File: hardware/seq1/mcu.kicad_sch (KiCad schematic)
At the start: 11 parts, among them SW10 SW_Push, SW11 SW_Push, SW9 PEC12R-3220F-S0024, U5 128x64 0.96" OLED I2C

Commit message: schematic and layout for v1 board
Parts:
- added C17: 1u, Capacitor_THT:C_Disc_D5.0mm_W2.5mm_P5.00mm, symbol Device:C
- added J6: Conn_02x06_Odd_Even, Connector_PinHeader_2.54mm:PinHeader_2x06_P2.54mm_Vertical, symbol Connector_Generic:Conn_02x06_Odd_Even
- added R19, R20: 4.7k, Resistor_THT:R_Axial_DIN0207_L6.3mm_D2.5mm_P10.16mm_Horizontal, symbol Device:R_US
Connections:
- net +3V3: now also R1.1, R2.1, C17.1, J6.1 (Pin_1), J6.2 (Pin_2), R19.1, R20.1; no longer R3.1, R4.1
- net +3V3_A: now also J6.3 (Pin_3)
- net +5V: now also J6.5 (Pin_5)
- net GATE: now also U1.14 (D2/PA14); no longer U1.30 (D13/PA17)
- net GND: now also SW9.S2, C17.2, J6.6 (Pin_6); no longer SW9.S1
- net MUX_ADDR0: now also U1.20 (D0/A6/PA11); no longer U1.29 (D12/PA19)
- net MUX_ADDR1: now also U1.21 (D1/A7/PA10); no longer U1.28 (D11/PA16)
- net MUX_ADDR2: now also U1.25 (D7/PA21); no longer U1.27 (D10/PA18)
- net N_MODE: now also SW10.2, U1.12 (D29/MOSI/PB10); no longer SW11.2, U1.14 (D2/PA14)
- net N_RUN: now also SW11.2; no longer SW10.2
- net ROT_SW: now also SW9.S1, U1.29 (D12/PA19); no longer SW9.S2, U1.10 (D19/A5/PB02)
- net RSWA: now also R3.1, U1.28 (D11/PA16); no longer R1.1, U1.11 (D30/SCK/PB11)
- net RSWB: now also R4.1, U1.27 (D10/PA18); no longer R2.1, U1.12 (D29/MOSI/PB10)
- net MCU_RST: now reaches U1.1 (RST)
- net MCU_RST: now also J6.4 (Pin_4)
- net D3_A9: now reaches U1.18 (D3/A9/PA09)
- net D3_A9: now also J6.12 (Pin_12)
- net D4_A8: now reaches U1.19 (D4/A8/PA08)
- net D4_A8: now also J6.10 (Pin_10)
- net at U1.22 (D26/SDA/PA22), U5.4 (SDA): now also R19.2
- net at U1.23 (D27/SCL/PA23), U5.3 (SCL): now also R20.2
- net D15_A1: now reaches U1.6 (D15/A1/PB08)
- net D15_A1: now also J6.7 (Pin_7)
- net D16_A2: now reaches U1.7 (D16/A2/PB09)
- net D16_A2: now also J6.9 (Pin_9)
- net D17_A3: now reaches U1.8 (D17/A3/PA04)
- net D17_A3: now also J6.11 (Pin_11)
- net at C1.1, R4.2, SW9.A: now also R2.2; no longer R1.2
- net at C2.1, R3.2, SW9.B: now also R1.2; no longer R2.2
- new net D13: J6.8 (Pin_8), U1.30 (D13/PA17)
- new net SYNC_IN: U1.10 (D19/A5/PB02)
- new net SYNC_OUT: U1.11 (D30/SCK/PB11)
- no-connect marks 0 -> 4
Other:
- moved on the sheet: U5

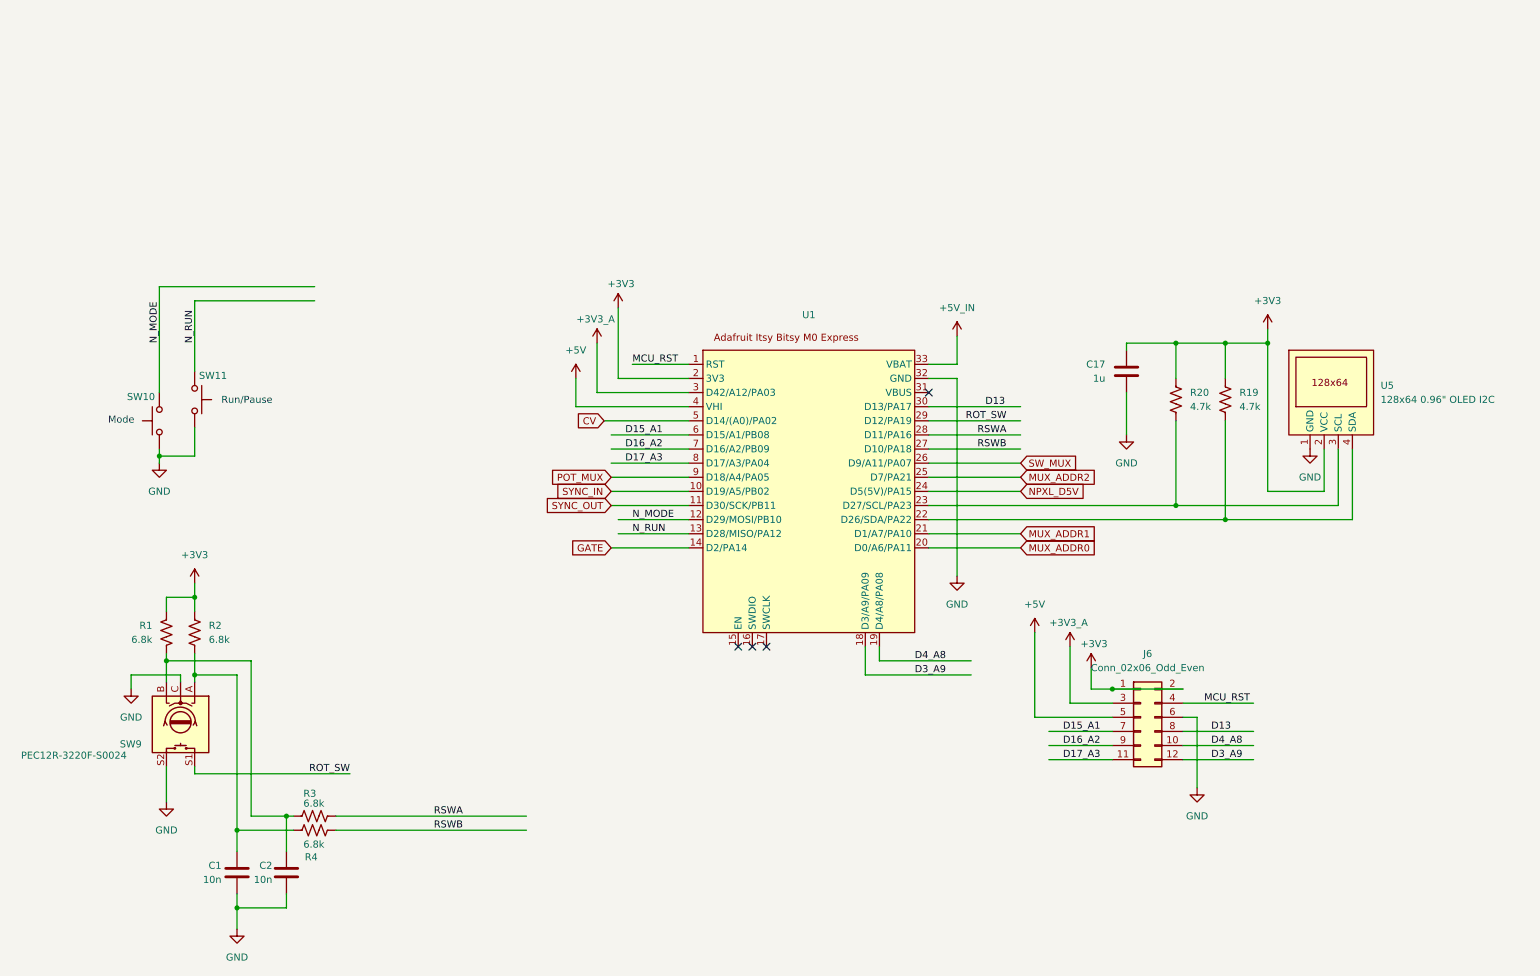
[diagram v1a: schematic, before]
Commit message: Adding support for the Itsy Bitsy M4 (SAMD51) architecture. Removed _util code and refactored to use the SAMD Utilities Library (SAMD_Utils.h). Compiles for QT Py M0, Itsy Bitsy M0 and M4
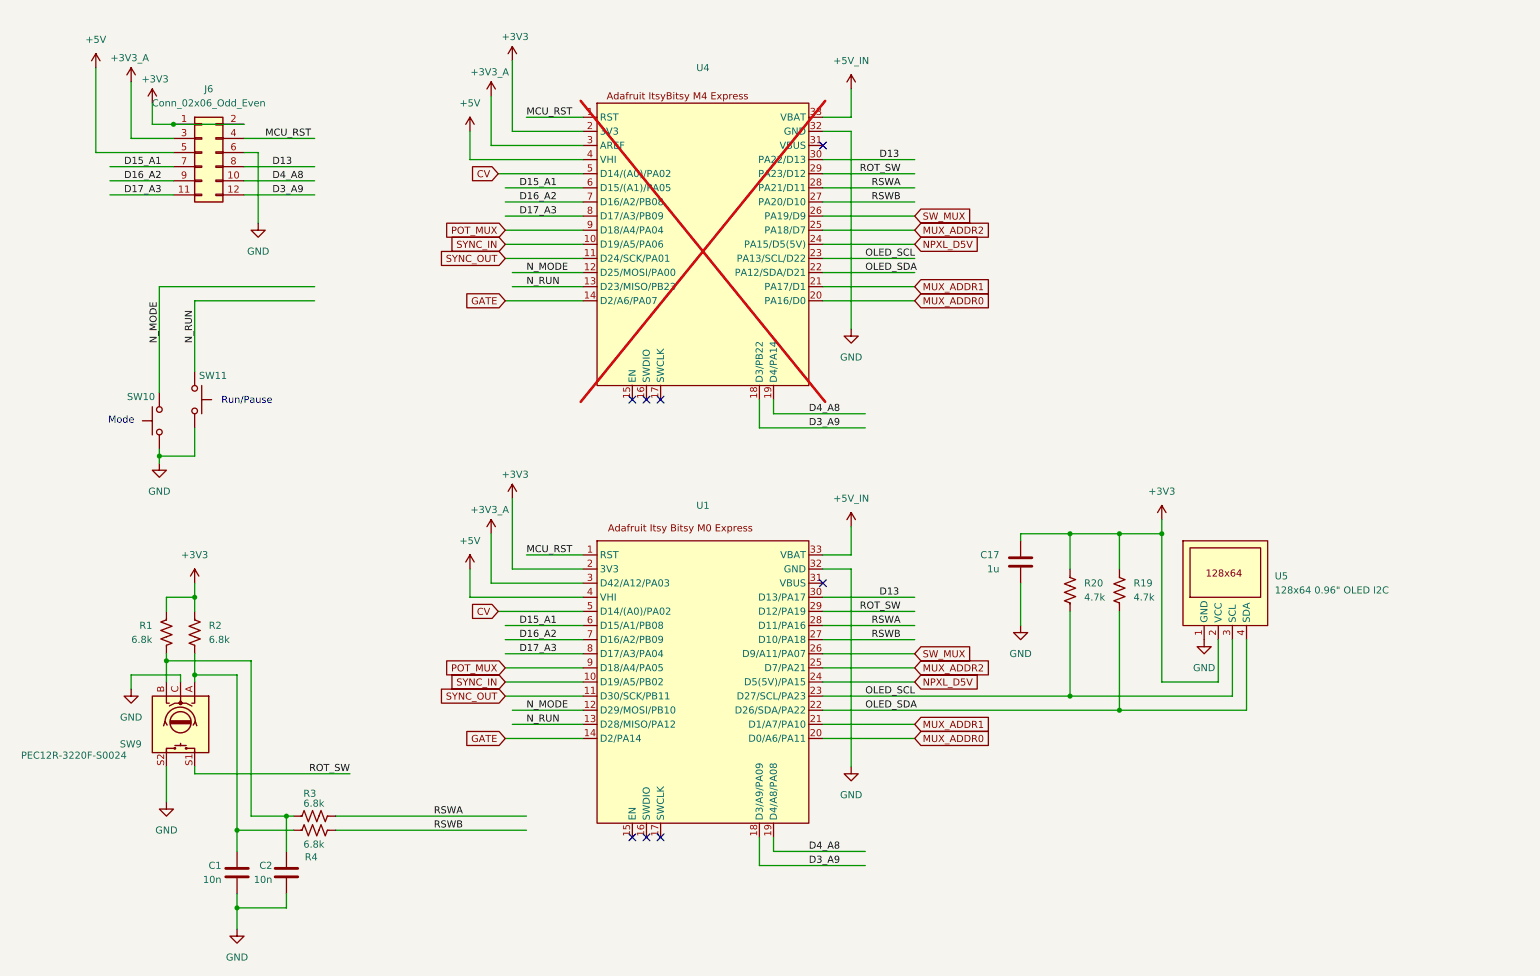
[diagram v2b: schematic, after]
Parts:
- added U4: ~, symbol MCU_Module_Custom:Adafruit_ItsyBitsy_M4_Express
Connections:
- net +3V3: now also U4.2 (3V3)
- net +3V3_A: now also U4.3 (AREF)
- net +5V: now also U4.4 (VHI)
- net +5V_IN: now also U4.33 (VBAT)
- net CV: now also U4.5 (D14/(A0)/PA02)
- net D13: now also U4.30 (PA22/D13)
- net D15_A1: now also U4.6 (D15/(A1)/PA05)
- net D16_A2: now also U4.7 (D16/A2/PB08)
- net D17_A3: now also U4.8 (D17/A3/PB09)
- net D3_A9: now also U4.18 (D3/PB22)
- net D4_A8: now also U4.19 (D4/PA14)
- net GATE: now also U4.14 (D2/A6/PA07)
- net GND: now also U4.32 (GND)
- net MCU_RST: now also U4.1 (RST)
- net MUX_ADDR0: now also U4.20 (PA16/D0)
- net MUX_ADDR1: now also U4.21 (PA17/D1)
- net MUX_ADDR2: now also U4.25 (PA18/D7)
- net NPXL_D5V: now also U4.24 (PA15/D5(5V))
- net N_MODE: now also U4.12 (D25/MOSI/PA00)
- net N_RUN: now also U4.13 (D23/MISO/PB23)
- net POT_MUX: now also U4.9 (D18/A4/PA04)
- net ROT_SW: now also U4.29 (PA23/D12)
- net RSWA: now also U4.28 (PA21/D11)
- net RSWB: now also U4.27 (PA20/D10)
- net SW_MUX: now also U4.26 (PA19/D9)
- net SYNC_IN: now also U4.10 (D19/A5/PA06)
- net SYNC_OUT: now also U4.11 (D24/SCK/PA01)
- net OLED_SDA: now reaches R19.2, U1.22 (D26/SDA/PA22), U5.4 (SDA)
- net OLED_SDA: now also U4.22 (PA12/SDA/D21)
- net OLED_SCL: now reaches R20.2, U1.23 (D27/SCL/PA23), U5.3 (SCL)
- net OLED_SCL: now also U4.23 (PA13/SCL/D22)
- no-connect marks 4 -> 8
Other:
- moved on the sheet: C17, J6, R19, R20, U1, U5

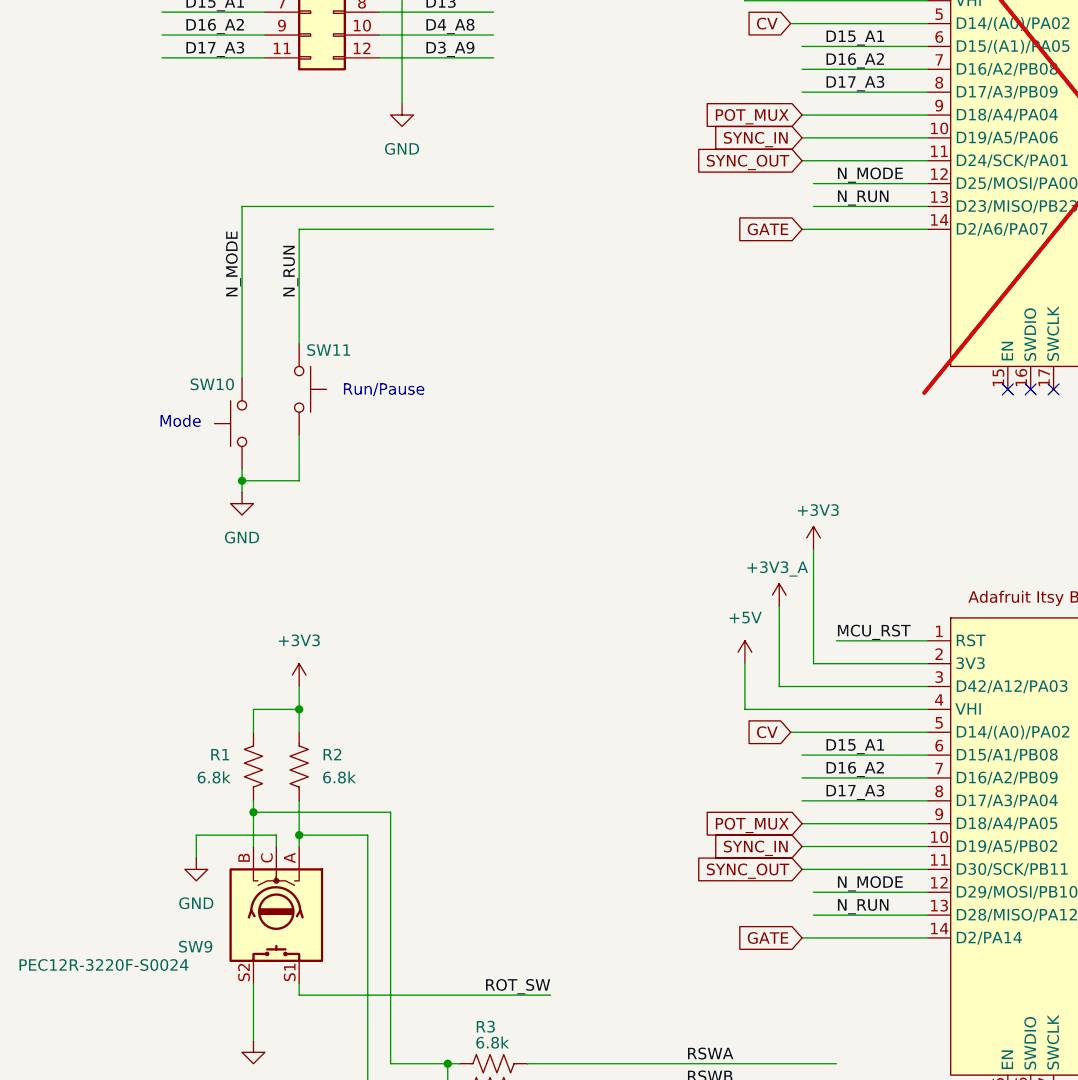
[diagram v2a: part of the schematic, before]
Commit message: bug in layout: order of pots reversed. Fixes for slide algo in controller, pin definitions and other fixes found in testing
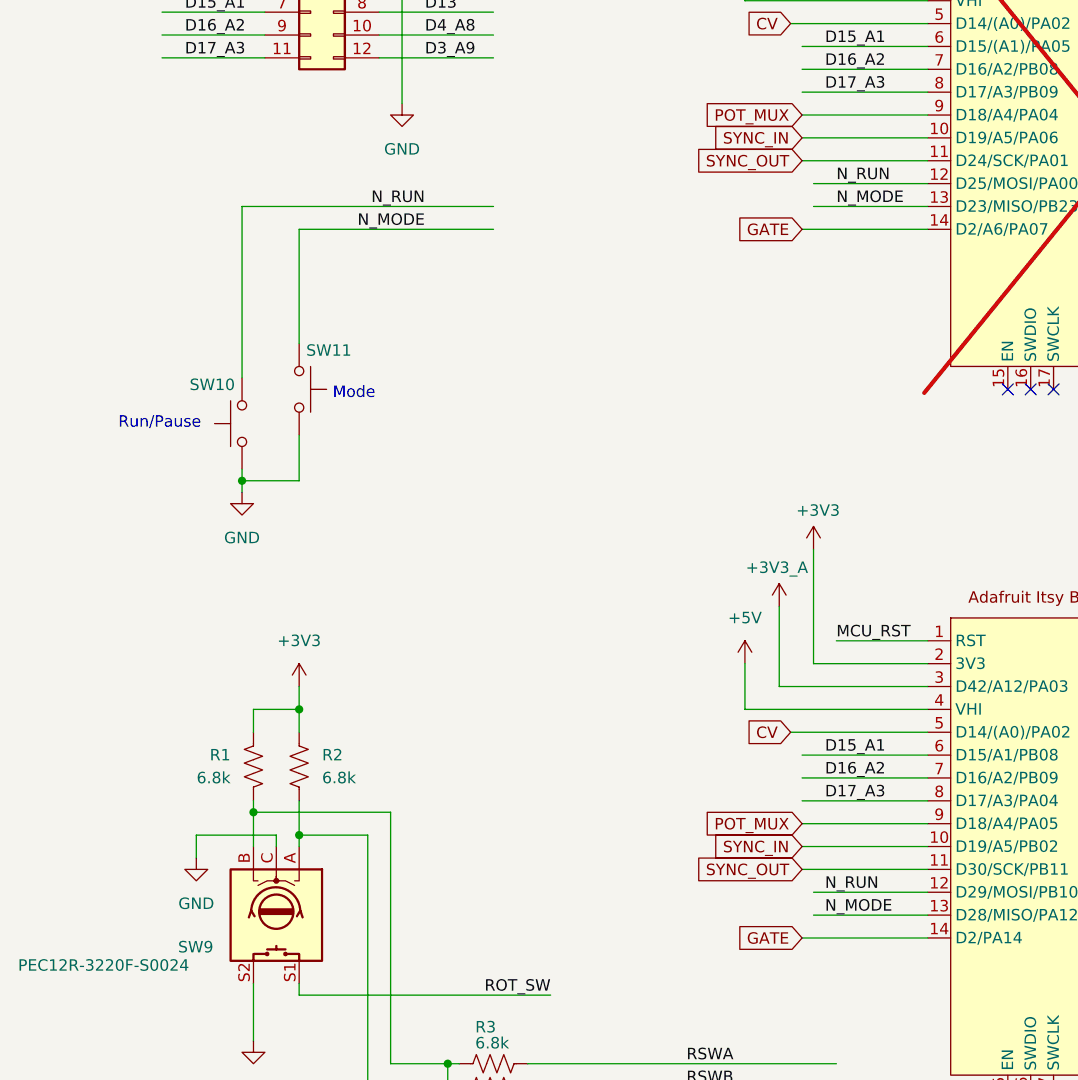
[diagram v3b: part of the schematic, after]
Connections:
- net N_MODE: now also SW11.2, U1.13 (D28/MISO/PA12), U4.13 (D23/MISO/PB23); no longer SW10.2, U1.12 (D29/MOSI/PB10), U4.12 (D25/MOSI/PA00)
- net N_RUN: now also SW10.2, U1.12 (D29/MOSI/PB10), U4.12 (D25/MOSI/PA00); no longer SW11.2, U1.13 (D28/MISO/PA12), U4.13 (D23/MISO/PB23)
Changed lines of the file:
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@@
 	(text "Mode"
 		(exclude_from_sim no)
-		(at 33.782 86.36 0)
+		(at 53.086 83.058 0)
 		(effects
 			(font
@@
 	(text "Run/Pause"
 		(exclude_from_sim no)
-		(at 56.388 82.804 0)
-		(effects
-			(font
-				(size 1.27 1.27)
-			)
+		(at 31.496 86.36 0)
+		(effects
+			(font
+				(size 1.27 1.27)
+			)
+		)
+	)
+	(label "N_MODE"
+		(at 105.41 140.97 0)
+		(fields_autoplaced yes)
+		(effects
+			(font
+				(size 1.27 1.27)
+			)
+			(justify left bottom)
 		)
 	)
@@
 	)
 	(label "N_RUN"
-		(at 106.68 140.97 0)
-		(fields_autoplaced yes)
-		(effects
-			(font
-				(size 1.27 1.27)
-			)
-			(justify left bottom)
-		)
-	)
-	(label "N_RUN"
-		(at 106.68 62.23 0)
-		(fields_autoplaced yes)
-		(effects
-			(font
-				(size 1.27 1.27)
-			)
-			(justify left bottom)
+		(at 60.96 62.23 180)
+		(fields_autoplaced yes)
+		(effects
+			(font
+				(size 1.27 1.27)
+			)
+			(justify right bottom)
 		)
 	)
@@
 		)
 	)
+	(label "N_RUN"
+		(at 105.41 138.43 0)
+		(fields_autoplaced yes)
+		(effects
+			(font
+				(size 1.27 1.27)
+			)
+			(justify left bottom)
+		)
+	)
+	(label "N_MODE"
+		(at 106.68 62.23 0)
+		(fields_autoplaced yes)
+		(effects
+			(font
+				(size 1.27 1.27)
+			)
+			(justify left bottom)
+		)
+	)
 	(label "ROT_SW"
 		(at 173.99 41.91 180)
@@
 		)
 	)
-	(label "N_RUN"
-		(at 46.99 72.39 90)
-		(fields_autoplaced yes)
-		(effects
-			(font
-				(size 1.27 1.27)
-			)
-			(justify left bottom)
-		)
-	)
 	(label "RSWA"
 		(at 173.99 44.45 180)
@@
 		)
 	)
+	(label "N_MODE"
+		(at 60.96 64.77 180)
+		(fields_autoplaced yes)
+		(effects
+			(font
+				(size 1.27 1.27)
+			)
+			(justify right bottom)
+		)
+	)
 	(label "D16_A2"
 		(at 105.41 46.99 0)
@@
 		)
 	)
-	(label "N_MODE"
-		(at 106.68 138.43 0)
-		(fields_autoplaced yes)
-		(effects
-			(font
-				(size 1.27 1.27)
-			)
-			(justify left bottom)
-		)
-	)
 	(label "RSWB"
 		(at 173.99 46.99 180)
@@
 		)
 	)
-	(label "N_MODE"
-		(at 40.64 72.39 90)
-		(fields_autoplaced yes)
-		(effects
-			(font
-				(size 1.27 1.27)
-			)
-			(justify left bottom)
-		)
-	)
 	(label "RSWB"
 		(at 173.99 125.73 180)
@@
 		)
 	)
-	(label "N_MODE"
+	(label "N_RUN"
 		(at 106.68 59.69 0)
 		(fields_autoplaced yes)
